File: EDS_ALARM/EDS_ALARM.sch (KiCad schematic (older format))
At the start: 24 parts, among them U1 STM32F411RETx

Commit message: Adding PIR sensor symbol and footprint
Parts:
- removed S1: EKMC1601111, symbol Sensor_Motion:EKMC1601111
- added PIR1: EKMC1601111, VZ-STANDARD, symbol EKMC1601111:EKMC1601111
- gave numbers to parts that had none: 5
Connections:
- wire segments 59 -> 65
- no-connect marks 3 -> 101
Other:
- moved on the sheet: C13

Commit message: Update EDS_ALARM.sch
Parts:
- added J3: 73412-0110, MOLEX_73412-0110, symbol U.FL:73412-0110
- PIR1: symbol EKMC1601111:EKMC1601111 -> EDS_ALARM-rescue:EKMC1601111-EKMC1601111
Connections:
- wire segments 65 -> 64
- no-connect marks 101 -> 58
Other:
- moved on the sheet: C13, C14, C15, C6, C7, J2, R1, R2, U1, Y1

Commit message: UPDATE
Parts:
- removed C14, C15: 18p, symbol Device:C
- removed R2: 10k, symbol Device:R
- removed U1: STM32F411RETx, Package_QFP:LQFP-64_10x10mm_P0.5mm, symbol MCU_ST_STM32F4:STM32F411RETx
- removed Y1: Crystal, symbol Device:Crystal
- added BZ?: Buzzer, symbol Device:Buzzer
- added CA1, CA2: 1u, symbol Device:C
- added SW1: SW_Push, symbol Switch:SW_Push
- C10, C7, C8, C9: value 100n -> 0.1u
- C11: value 100n -> 1u
- C12: value 4,7u -> 0.1u
- C13: value 4,7u -> 100N
- C6: value 1u -> 10u
- J3: footprint MOLEX_73412-0110 -> Connector_Coaxial:U.FL_Molex_MCRF_73412-0110_Vertical
- PIR1: footprint VZ-STANDARD -> (none)
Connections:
- net +3V3: now also J2.1 (Pin_1), U2.32 (VREF+), U2.4 (VDD_USB), U2.48 (VDD_TCXO), U2.5 (VDD_MCU), U2.6 (VDD_RF); no longer C12.1, R1.2
- net GND: now also J2.3 (Pin_3), J3.2 (GND), J3.3 (GND), J3.4 (GND), R1.2, U2.25 (GND), U2.27 (GND), U2.3 (GND), U2.44 (GND), U2.49 (GND), U2.50 (GND), U2.51 (GND), U2.52 (GND), U2.53 (GND), U2.54 (GND), U2.55 (GND), U2.56 (GND), U2.57 (GND), U2.7 (GND), CA1.2, CA2.2, SW1.1; no longer C13.2
- net at C13.1: now also J3.1 (SIG), CA2.1
- net at R1.1: now also U2.43 (BOOT0)
- net SWCLK: now reaches J2.2 (Pin_2)
- net SWCLK: now also U2.42 (PA14/SWCLK)
- net SWDIO: now reaches J2.4 (Pin_4)
- net SWDIO: now also U2.41 (PA13/SWDIO)
- net NRST: now reaches J2.5 (Pin_5)
- net NRST: now also C12.1, U2.34 (~MCU_RST), SW1.2
- net ADC4: now reaches U2.22 (PA4/ADC4/DAC1)
- net ADC4: now also PIR1.2
- net at U2.26 (ANT): now also C13.2, CA1.1
- no-connect marks 58 -> 4
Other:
- moved on the sheet: J2, J3, PIR1, U2

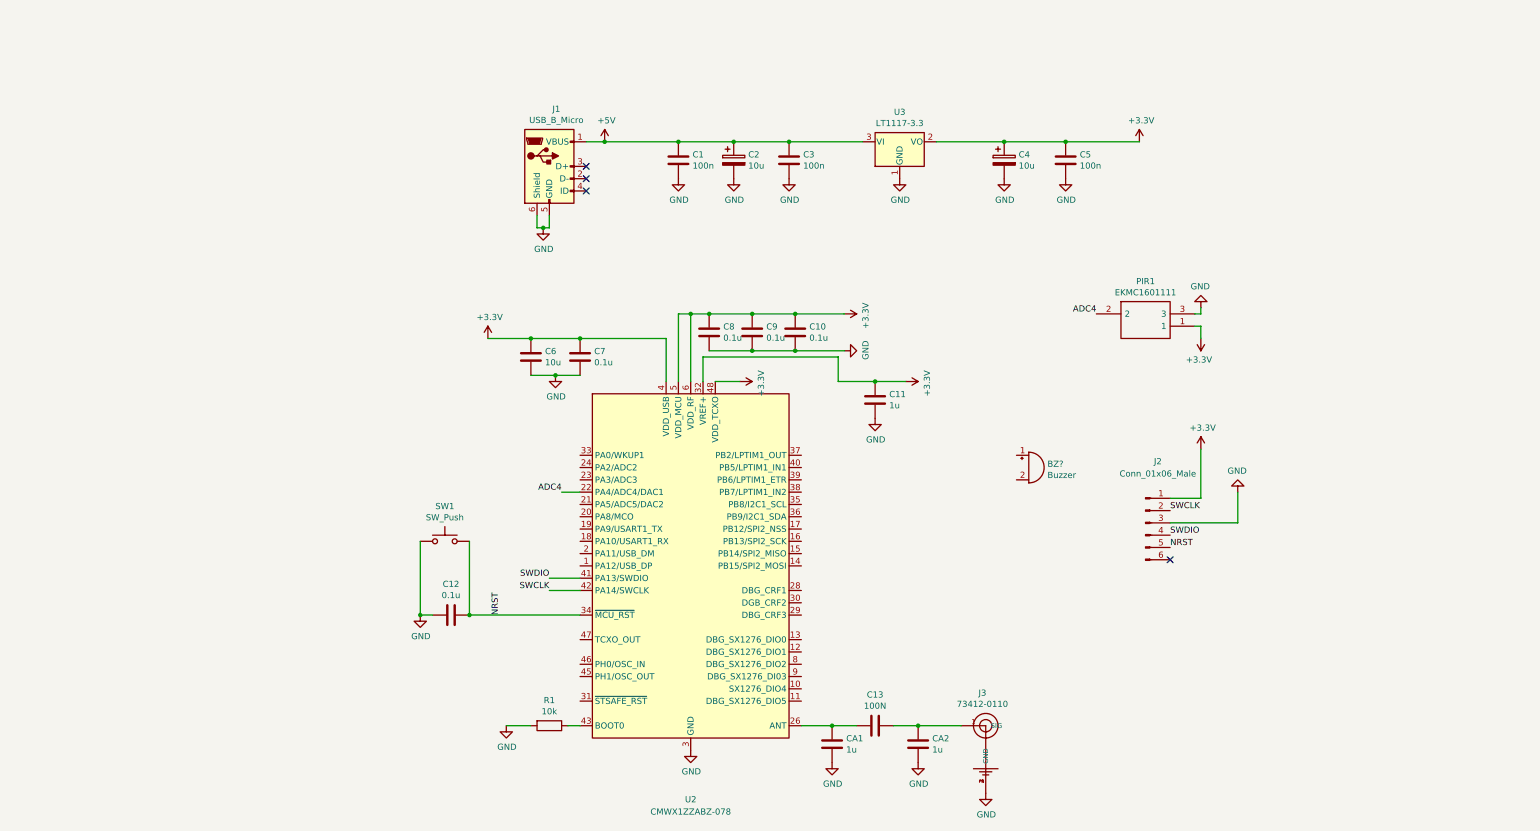
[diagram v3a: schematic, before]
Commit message: Adding correct footprints to corresponding symbols, adding cristal
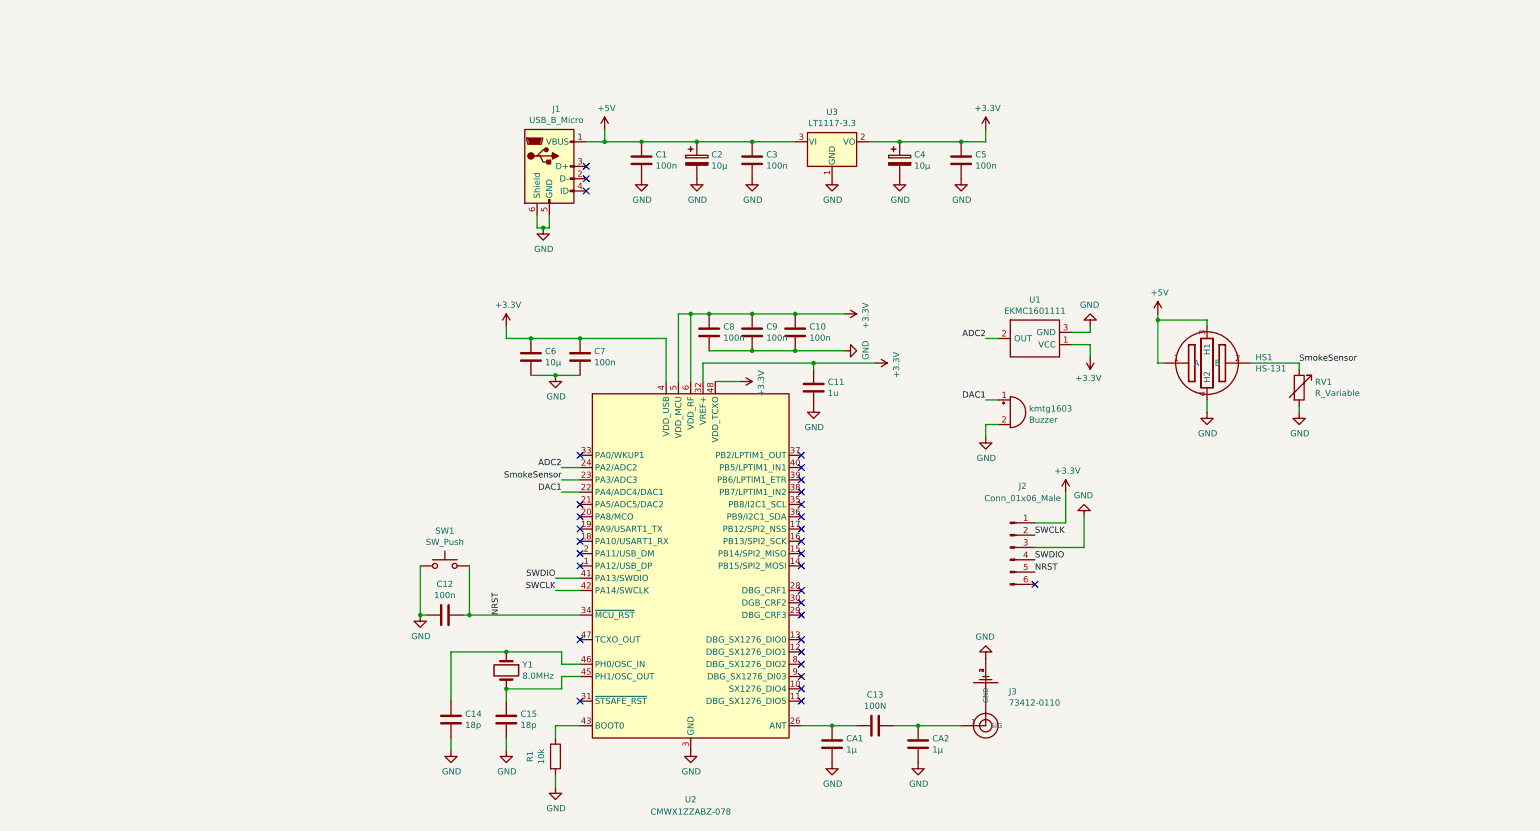
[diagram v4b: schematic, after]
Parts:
- removed J3: 73412-0110, Connector_Coaxial:U.FL_Molex_MCRF_73412-0110_Vertical, symbol U.FL:73412-0110
- removed PIR1: EKMC1601111, symbol EDS_ALARM-rescue:EKMC1601111-EKMC1601111
- added C14, C15: 18p, Capacitor_SMD:C_0805_2012Metric_Pad1.15x1.40mm_HandSolder, symbol Device:C
- added HS1: HS-131, symbol HS-131:HS-131
- added J3: 73412-0110, Connector_Coaxial:U.FL_Molex_MCRF_73412-0110_Vertical, symbol 73412-0110:73412-0110
- added RV1: R_Variable, symbol Device:R_Variable
- added U1: EKMC1601111, EKMC1601111:VZ-STANDARD, symbol EKMC1601111:EKMC1601111
- added Y1: 8.0MHz, Crystal:Crystal_HC49-U-3Pin_Vertical, symbol Device:Crystal
- C1, C11, C13, C3, C5: footprint (none) -> Capacitor_SMD:C_0805_2012Metric_Pad1.15x1.40mm_HandSolder
- C10, C12, C7, C8, C9: value 0.1u -> 100n; footprint (none) -> Capacitor_SMD:C_0805_2012Metric_Pad1.15x1.40mm_HandSolder
- C2, C4: value 10u -> 10µ; footprint (none) -> Capacitor_SMD:CP_Elec_5x4.4
- C6: value 10u -> 10µ; footprint (none) -> Capacitor_SMD:C_0805_2012Metric_Pad1.15x1.40mm_HandSolder
- CA1, CA2: value 1u -> 1µ; footprint (none) -> Capacitor_SMD:C_0805_2012Metric_Pad1.15x1.40mm_HandSolder
- J1: footprint (none) -> Connector_USB:USB_Mini-B_Lumberg_2486_01_Horizontal
- J2: footprint (none) -> Connector_PinHeader_2.54mm:PinHeader_1x06_P2.54mm_Vertical
- R1: footprint (none) -> Resistor_SMD:R_0805_2012Metric_Pad1.15x1.40mm_HandSolder
- U3: footprint (none) -> Package_TO_SOT_SMD:SOT-223
- gave numbers to parts that had none: 1
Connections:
- net ADC4 is gone; now on net DAC1: U2.22 (PA4/ADC4/DAC1)
- net +3V3: now also U1.1 (VCC)
- net +5V: now also HS1.1 (A), HS1.3 (H1)
- net GND: now also kmtg1603.2 (+), C14.2, C15.2, HS1.4 (H2), J3.2 (GND), J3.3 (GND), J3.4 (GND), RV1.2, U1.3 (GND)
- net at C13.1, CA2.1: now also J3.1 (SIG)
- net SmokeSensor: now reaches U2.23 (PA3/ADC3)
- net SmokeSensor: now also HS1.2 (B), RV1.1
- net ADC2: now reaches U2.24 (PA2/ADC2)
- net ADC2: now also U1.2 (OUT)
- net at U2.45 (PH1/OSC_OUT): now also C15.1, Y1.2
- net at U2.46 (PH0/OSC_IN): now also C14.1, Y1.1
- net DAC1: now reaches kmtg1603.1 (-)
- no-connect marks 4 -> 32
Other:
- moved on the sheet: C1, C11, C12, C2, C3, C4, C5, J2, R1, SW1, U3, kmtg1603
